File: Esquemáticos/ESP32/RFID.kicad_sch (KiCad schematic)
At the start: 1 part

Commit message: Arreglando los bugs xd
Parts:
- removed J?: Conn_RFID_SPI, symbol Connector:Conn_01x08_Female
- added U1: RFID_RC522, symbol libreria_raul:RFID_RC522
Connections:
- net 3.3V: now also U1.8 (3.3V)
- net GND: now also U1.6 (GND)
- net MISO: now also U1.4 (MISO)
- net MOSI: now also U1.3 (MOSI)
- net SCK: now also U1.2 (SCK)
- net SS: now also U1.1 (SS)
- no-connect marks 1 -> 0
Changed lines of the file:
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@@
 (kicad_sch (version 20211123) (generator eeschema)
   (paper "A4")
-  (no_connect (at 142.24 104.14))
-  (wire (pts (xy 140.97 96.52) (xy 142.24 96.52))
+  (wire (pts (xy 133.35 99.06) (xy 138.43 99.06))
     (stroke (width 0) (type default) (color 0 0 0 0))
   )
-  (polyline (pts (xy 125.73 116.84) (xy 125.73 88.9))
+  (polyline (pts (xy 124.46 116.84) (xy 124.46 88.9))
     (stroke (width 0) (type default) (color 0 0 0 0))
   )
-  (wire (pts (xy 140.97 109.22) (xy 142.24 109.22))
+  (wire (pts (xy 138.43 105.41) (xy 135.89 105.41))
     (stroke (width 0) (type default) (color 0 0 0 0))
   )
-  (polyline (pts (xy 173.99 116.84) (xy 125.73 116.84))
+  (polyline (pts (xy 177.8 116.84) (xy 124.46 116.84))
     (stroke (width 0) (type default) (color 0 0 0 0))
   )
-  (wire (pts (xy 140.97 111.76) (xy 142.24 111.76))
+  (wire (pts (xy 133.35 106.68) (xy 138.43 106.68))
     (stroke (width 0) (type default) (color 0 0 0 0))
   )
-  (polyline (pts (xy 173.99 88.9) (xy 173.99 116.84))
+  (polyline (pts (xy 177.8 88.9) (xy 177.8 116.84))
     (stroke (width 0) (type default) (color 0 0 0 0))
   )
-  (wire (pts (xy 140.97 101.6) (xy 142.24 101.6))
+  (wire (pts (xy 133.35 101.6) (xy 138.43 101.6))
     (stroke (width 0) (type default) (color 0 0 0 0))
   )
-  (polyline (pts (xy 125.73 88.9) (xy 173.99 88.9))
+  (wire (pts (xy 138.43 104.14) (xy 134.62 104.14))
     (stroke (width 0) (type default) (color 0 0 0 0))
   )
-  (wire (pts (xy 140.97 99.06) (xy 142.24 99.06))
+  (polyline (pts (xy 124.46 88.9) (xy 177.8 88.9))
     (stroke (width 0) (type default) (color 0 0 0 0))
   )
-  (wire (pts (xy 140.97 93.98) (xy 142.24 93.98))
+  (wire (pts (xy 133.35 100.33) (xy 138.43 100.33))
+    (stroke (width 0) (type default) (color 0 0 0 0))
+  )
+  (wire (pts (xy 133.35 97.79) (xy 138.43 97.79))
     (stroke (width 0) (type default) (color 0 0 0 0))
   )
@@
     (effects (font (size 1.27 1.27)) (justify left bottom))
   )
-  (text "Pines RFID RC522\nProtocolo SPI" (at 143.51 86.36 180)
-    (effects (font (size 1.27 1.27)) (justify right bottom))
+  (text "Pines RFID RC522\nProtocolo SPI" (at 124.46 121.92 0)
+    (effects (font (size 1.27 1.27)) (justify left bottom))
   )
-  (hierarchical_label "MOSI" (shape output) (at 140.97 99.06 180)
+  (hierarchical_label "MOSI" (shape output) (at 133.35 100.33 180)
     (effects (font (size 1.27 1.27)) (justify right))
   )
-  (hierarchical_label "MISO" (shape output) (at 140.97 101.6 180)
+  (hierarchical_label "MISO" (shape output) (at 133.35 101.6 180)
     (effects (font (size 1.27 1.27)) (justify right))
   )
-  (hierarchical_label "SS" (shape input) (at 140.97 93.98 180)
+  (hierarchical_label "SS" (shape input) (at 133.35 97.79 180)
     (effects (font (size 1.27 1.27)) (justify right))
   )
-  (hierarchical_label "SCK" (shape input) (at 140.97 96.52 180)
+  (hierarchical_label "SCK" (shape input) (at 133.35 99.06 180)
     (effects (font (size 1.27 1.27)) (justify right))
   )
-  (hierarchical_label "3.3V" (shape input) (at 140.97 111.76 180)
+  (hierarchical_label "3.3V" (shape input) (at 133.35 106.68 180)
     (effects (font (size 1.27 1.27)) (justify right))
   )
-  (hierarchical_label "RST" (shape input) (at 140.97 109.22 180)
+  (hierarchical_label "RST" (shape input) (at 134.62 105.41 180)
     (effects (font (size 1.27 1.27)) (justify right))
   )
-  (symbol (lib_id "Connector:Conn_01x08_Female") (at 147.32 101.6 0) (unit 1)
+  (symbol (lib_id "libreria_raul:RFID_RC522") (at 149.86 93.98 0) (unit 1)
     (in_bom yes) (on_board yes) (fields_autoplaced)
-    (property "Reference" "J?" (id 0) (at 148.59 101.5999 0)
+    (property "Reference" "U1" (id 0) (at 163.83 101.5999 0)
       (effects (font (size 1.27 1.27)) (justify left))
     )
-    (property "Value" "Conn_RFID_SPI" (id 1) (at 148.59 104.1399 0)
+    (property "Value" "RFID_RC522" (id 1) (at 163.83 104.1399 0)
       (effects (font (size 1.27 1.27)) (justify left))
     )
-    (property "Footprint" "" (id 2) (at 147.32 101.6 0)
+    (property "Footprint" "" (id 2) (at 149.86 93.98 0)
       (effects (font (size 1.27 1.27)) hide)
     )
-    (property "Datasheet" "~" (id 3) (at 147.32 101.6 0)
+    (property "Datasheet" "" (id 3) (at 149.86 93.98 0)
       (effects (font (size 1.27 1.27)) hide)
     )
@@
     (pin "8")
   )
-  (symbol (lib_id "power:GND") (at 142.24 106.68 270) (unit 1)
+  (symbol (lib_id "power:GND") (at 134.62 104.14 270) (unit 1)
     (in_bom yes) (on_board yes) (fields_autoplaced)
-    (property "Reference" "#PWR0115" (id 0) (at 135.89 106.68 0)
+    (property "Reference" "#PWR?" (id 0) (at 128.27 104.14 0)
       (effects (font (size 1.27 1.27)) hide)
     )
-    (property "Value" "GND" (id 1) (at 138.43 106.6799 90)
+    (property "Value" "GND" (id 1) (at 130.81 104.1399 90)
       (effects (font (size 1.27 1.27)) (justify right))
     )
-    (property "Footprint" "" (id 2) (at 142.24 106.68 0)
+    (property "Footprint" "" (id 2) (at 134.62 104.14 0)
       (effects (font (size 1.27 1.27)) hide)
     )
-    (property "Datasheet" "" (id 3) (at 142.24 106.68 0)
+    (property "Datasheet" "" (id 3) (at 134.62 104.14 0)
       (effects (font (size 1.27 1.27)) hide)
     )

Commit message: actualización raul_2
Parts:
- U1: footprint (none) -> Library_raul:RFID_RC522
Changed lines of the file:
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@@
       (effects (font (size 1.27 1.27)) (justify left))
     )
-    (property "Footprint" "" (id 2) (at 149.86 93.98 0)
+    (property "Footprint" "Library_raul:RFID_RC522" (id 2) (at 149.86 93.98 0)
       (effects (font (size 1.27 1.27)) hide)
     )

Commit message: gente creo q borre cosas sin querer :(
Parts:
- U1: footprint Library_raul:RFID_RC522 -> Connector_JST:JST_EH_B8B-EH-A_1x08_P2.50mm_Vertical
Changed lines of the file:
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@@
       (effects (font (size 1.27 1.27)) (justify left))
     )
-    (property "Footprint" "Library_raul:RFID_RC522" (id 2) (at 149.86 93.98 0)
+    (property "Footprint" "Connector_JST:JST_EH_B8B-EH-A_1x08_P2.50mm_Vertical" (id 2) (at 149.86 93.98 0)
       (effects (font (size 1.27 1.27)) hide)
     )

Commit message: Support
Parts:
- renumbered U1 to U8
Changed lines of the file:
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@@
   (symbol (lib_id "libreria_raul:RFID_RC522") (at 149.86 93.98 0) (unit 1)
     (in_bom yes) (on_board yes) (fields_autoplaced)
-    (property "Reference" "U1" (id 0) (at 163.83 101.5999 0)
+    (property "Reference" "U8" (id 0) (at 163.83 101.5999 0)
       (effects (font (size 1.27 1.27)) (justify left))
     )
@@
   (symbol (lib_id "power:GND") (at 134.62 104.14 270) (unit 1)
     (in_bom yes) (on_board yes) (fields_autoplaced)
-    (property "Reference" "#PWR?" (id 0) (at 128.27 104.14 0)
+    (property "Reference" "#PWR012" (id 0) (at 128.27 104.14 0)
       (effects (font (size 1.27 1.27)) hide)
     )

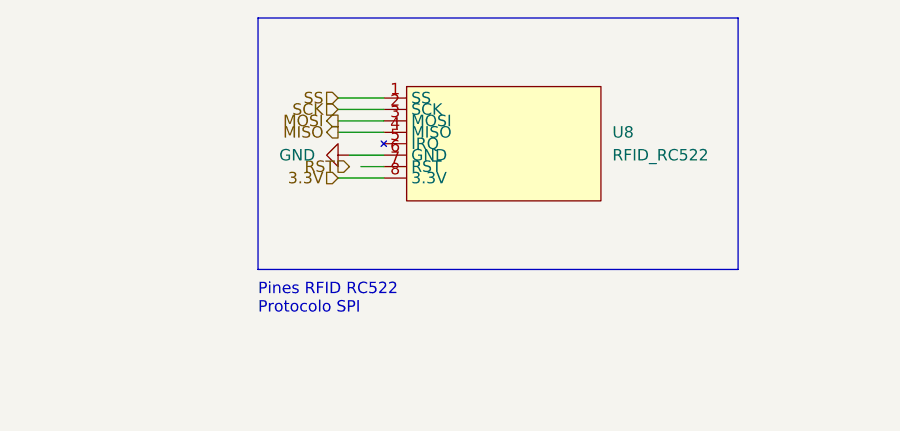
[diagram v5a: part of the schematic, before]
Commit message: Etiquetas globales para alimentación añadidas
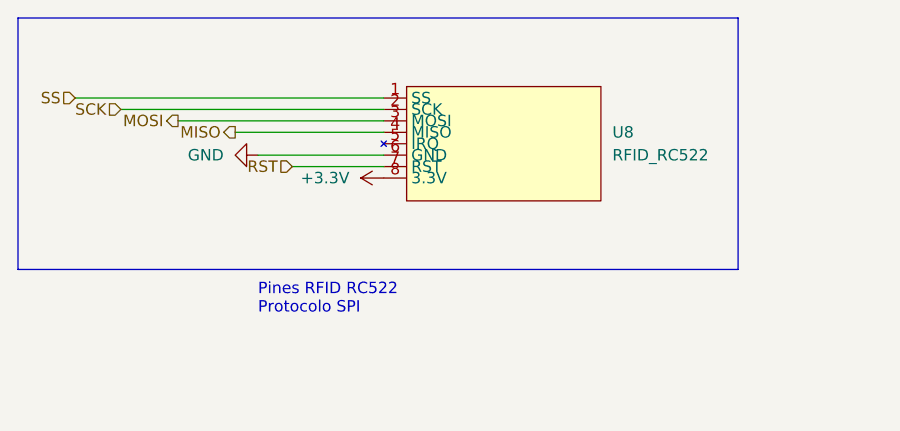
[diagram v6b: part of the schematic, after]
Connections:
- net RST: now also U8.7 (RST)
- net 3.3V renamed +3.3V
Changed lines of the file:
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@@
 (kicad_sch (version 20211123) (generator eeschema)
   (paper "A4")
-  (wire (pts (xy 133.35 99.06) (xy 138.43 99.06))
+  (wire (pts (xy 109.22 99.06) (xy 138.43 99.06))
     (stroke (width 0) (type default) (color 0 0 0 0))
   )
-  (polyline (pts (xy 124.46 116.84) (xy 124.46 88.9))
+  (polyline (pts (xy 97.79 116.84) (xy 97.79 88.9))
     (stroke (width 0) (type default) (color 0 0 0 0))
   )
-  (wire (pts (xy 138.43 105.41) (xy 135.89 105.41))
-    (stroke (width 0) (type default) (color 0 0 0 0))
-  )
-  (polyline (pts (xy 177.8 116.84) (xy 124.46 116.84))
-    (stroke (width 0) (type default) (color 0 0 0 0))
-  )
-  (wire (pts (xy 133.35 106.68) (xy 138.43 106.68))
+  (polyline (pts (xy 177.8 116.84) (xy 97.79 116.84))
     (stroke (width 0) (type default) (color 0 0 0 0))
   )
@@
     (stroke (width 0) (type default) (color 0 0 0 0))
   )
-  (wire (pts (xy 133.35 101.6) (xy 138.43 101.6))
+  (wire (pts (xy 128.27 105.41) (xy 138.43 105.41))
     (stroke (width 0) (type default) (color 0 0 0 0))
   )
-  (wire (pts (xy 138.43 104.14) (xy 134.62 104.14))
+  (wire (pts (xy 121.92 101.6) (xy 138.43 101.6))
     (stroke (width 0) (type default) (color 0 0 0 0))
   )
-  (polyline (pts (xy 124.46 88.9) (xy 177.8 88.9))
+  (wire (pts (xy 124.46 104.14) (xy 138.43 104.14))
     (stroke (width 0) (type default) (color 0 0 0 0))
   )
-  (wire (pts (xy 133.35 100.33) (xy 138.43 100.33))
+  (polyline (pts (xy 97.79 88.9) (xy 177.8 88.9))
     (stroke (width 0) (type default) (color 0 0 0 0))
   )
-  (wire (pts (xy 133.35 97.79) (xy 138.43 97.79))
+  (wire (pts (xy 115.57 100.33) (xy 138.43 100.33))
+    (stroke (width 0) (type default) (color 0 0 0 0))
+  )
+  (wire (pts (xy 104.14 97.79) (xy 138.43 97.79))
     (stroke (width 0) (type default) (color 0 0 0 0))
   )
@@
     (effects (font (size 1.27 1.27)) (justify left bottom))
   )
-  (hierarchical_label "MOSI" (shape output) (at 133.35 100.33 180)
+  (hierarchical_label "MOSI" (shape output) (at 115.57 100.33 180)
     (effects (font (size 1.27 1.27)) (justify right))
   )
-  (hierarchical_label "MISO" (shape output) (at 133.35 101.6 180)
+  (hierarchical_label "MISO" (shape output) (at 121.92 101.6 180)
     (effects (font (size 1.27 1.27)) (justify right))
   )
-  (hierarchical_label "SS" (shape input) (at 133.35 97.79 180)
+  (hierarchical_label "SS" (shape input) (at 104.14 97.79 180)
     (effects (font (size 1.27 1.27)) (justify right))
   )
-  (hierarchical_label "SCK" (shape input) (at 133.35 99.06 180)
+  (hierarchical_label "SCK" (shape input) (at 109.22 99.06 180)
     (effects (font (size 1.27 1.27)) (justify right))
   )
-  (hierarchical_label "3.3V" (shape input) (at 133.35 106.68 180)
-    (effects (font (size 1.27 1.27)) (justify right))
-  )
-  (hierarchical_label "RST" (shape input) (at 134.62 105.41 180)
+  (hierarchical_label "RST" (shape input) (at 128.27 105.41 180)
     (effects (font (size 1.27 1.27)) (justify right))
   )
@@
     (pin "8")
   )
-  (symbol (lib_id "power:GND") (at 134.62 104.14 270) (unit 1)
+  (symbol (lib_id "power:+3.3V") (at 138.43 106.68 90) (unit 1)
     (in_bom yes) (on_board yes) (fields_autoplaced)
-    (property "Reference" "#PWR012" (id 0) (at 128.27 104.14 0)
+    (property "Reference" "#PWR029" (id 0) (at 142.24 106.68 0)
       (effects (font (size 1.27 1.27)) hide)
     )
-    (property "Value" "GND" (id 1) (at 130.81 104.1399 90)
+    (property "Value" "+3.3V" (id 1) (at 134.62 106.6799 90)
+      (effects (font (size 1.27 1.27)) (justify left))
+    )
+    (property "Footprint" "" (id 2) (at 138.43 106.68 0)
+      (effects (font (size 1.27 1.27)) hide)
+    )
+    (property "Datasheet" "" (id 3) (at 138.43 106.68 0)
+      (effects (font (size 1.27 1.27)) hide)
+    )
+    (pin "1")
+  )
+  (symbol (lib_id "power:GND") (at 124.46 104.14 270) (unit 1)
+    (in_bom yes) (on_board yes) (fields_autoplaced)
+    (property "Reference" "#PWR012" (id 0) (at 118.11 104.14 0)
+      (effects (font (size 1.27 1.27)) hide)
+    )
+    (property "Value" "GND" (id 1) (at 120.65 104.1399 90)
       (effects (font (size 1.27 1.27)) (justify right))
     )
-    (property "Footprint" "" (id 2) (at 134.62 104.14 0)
+    (property "Footprint" "" (id 2) (at 124.46 104.14 0)
       (effects (font (size 1.27 1.27)) hide)
     )
-    (property "Datasheet" "" (id 3) (at 134.62 104.14 0)
+    (property "Datasheet" "" (id 3) (at 124.46 104.14 0)
       (effects (font (size 1.27 1.27)) hide)
     )
